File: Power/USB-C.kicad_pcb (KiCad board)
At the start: 2 copper layers, 80 x 30 mm, 27 parts, among them J1 USB_C_Receptacle_PowerOnly_6P, J2 Barrel_Jack_Switch, J3 Barrel_Jack_Switch, J4 Barrel_Jack_Switch, J5 Barrel_Jack_Switch, U1 HUSB237, U2 TPS73801

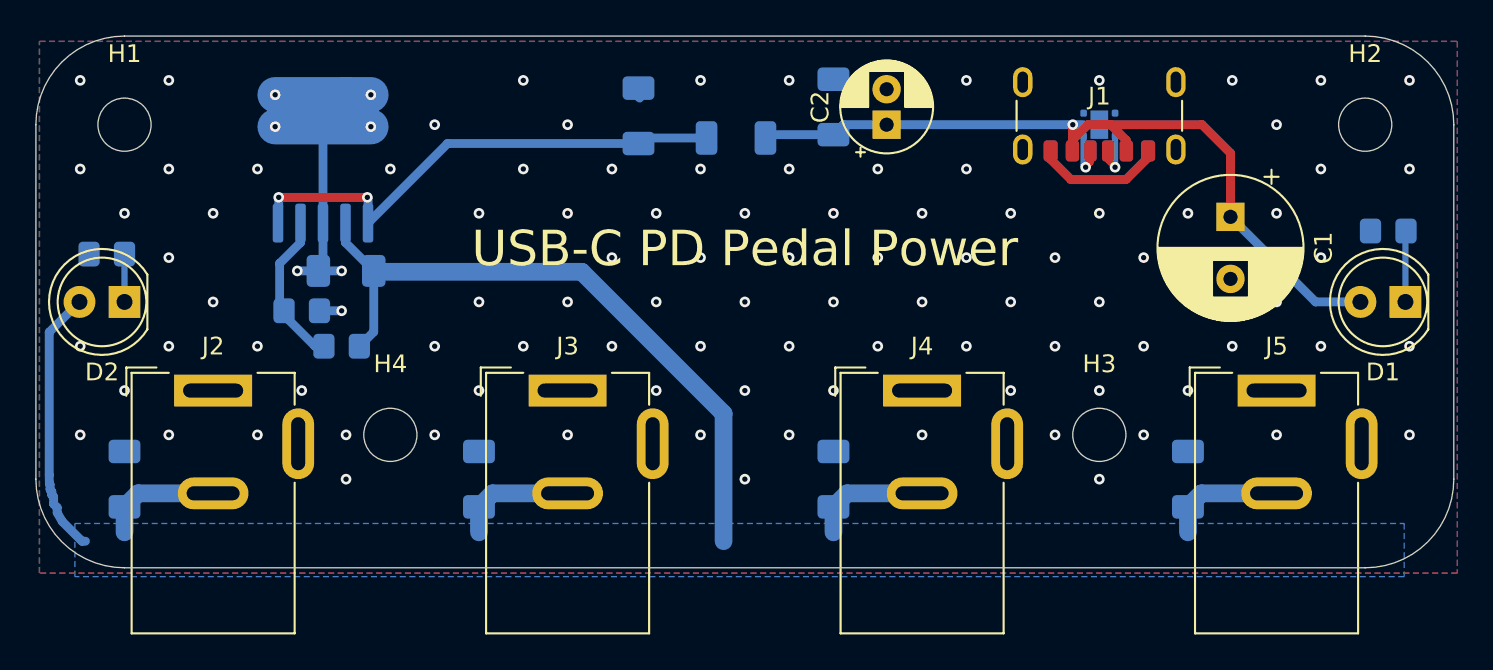
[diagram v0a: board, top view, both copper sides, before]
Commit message: Make a switchable combo version of the USB-PD power board
So this was triggered partly by me noticing that my USB PD sources are
very inconsistent when it comes to 12V output that the original board
requested.

Several of my wall chargers do 15V but not 12V.  Of course, then some of
my battery packs are the reverse, and do 12V but not 15V output.

So there is no single thing that works for all common cases.  But 15V is
the more common option, and is required by the PD specs for anything
that claims to be 45W or more.  12V is entirely optional.

End result: add a switch to pick whether the power board requests 12V or
15V from the USB-C PD source.

And since 15V is now an option, add another LDO, and a switch to make
that LDO generate either 9V or 12V output (as per commit eb97091: "Add a
USB-C pedal power board" that already mentioned this option).

Connect the LDOs to two ports each, which also results in a certain
amount of isolation.

End result: the first two ports always output 9V, while the second two
ports can optionally provide 12V output if your USB-PD source does 15V.

The "switch" is either just a pin header with a jumper, or one of the
small slide switches that I have.  We're not doing anything fancy here.

Signed-off-by: Linus Torvalds <torvalds@linux-foundation.org>
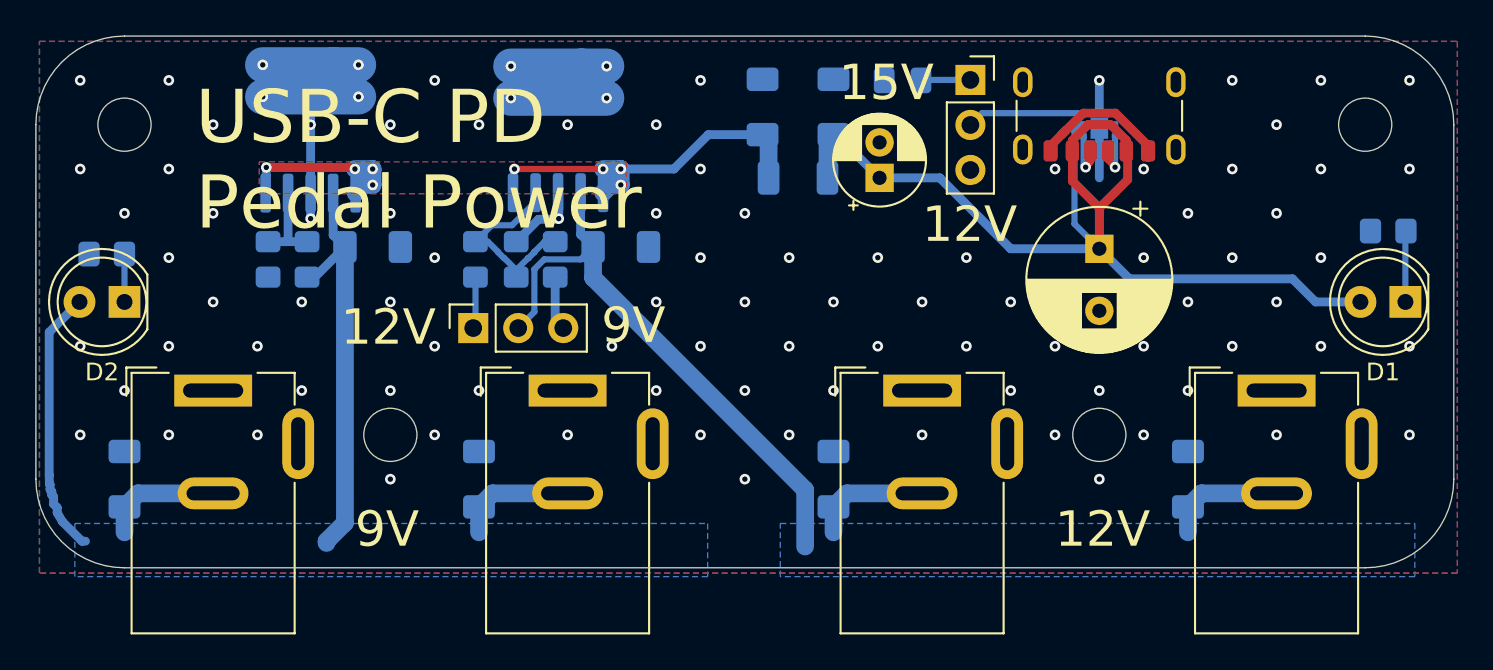
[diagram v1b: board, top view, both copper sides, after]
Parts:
- added C11: 22uF, Capacitor_SMD:C_1206_3216Metric_Pad1.33x1.80mm_HandSolder, B.Cu at (83.0, 61.9)
- added C5: 4.7nF, Capacitor_SMD:C_0805_2012Metric_Pad1.18x1.45mm_HandSolder, B.Cu at (98.9, 52.5)
- added R3: 13k, Resistor_SMD:R_0805_2012Metric_Pad1.20x1.40mm_HandSolder, B.Cu at (79.3, 62.6)
- added R4: 18k, Resistor_SMD:R_0805_2012Metric_Pad1.20x1.40mm_HandSolder, B.Cu at (74.8, 62.6)
- added R7: 2k, Resistor_SMD:R_0805_2012Metric_Pad1.20x1.40mm_HandSolder, B.Cu at (77.1, 62.6)
- added SW1: 15v12, Connector_PinSocket_2.54mm:PinSocket_1x03_P2.54mm_Vertical, F.Cu at (102.7, 52.5)
- added SW2: 12v9, Connector_PinSocket_2.54mm:PinSocket_1x03_P2.54mm_Vertical, F.Cu at (74.7, 66.5)
- added U2: TPS73801, Package_TO_SOT_SMD:SOT-223-6, B.Cu at (79.5, 55.7)
- C10: renamed from C9; value 10uF -> 22uF
- C6: renamed from C5; value 10uF -> 22uF
- C7: renamed from C6; value 10uF -> 22uF
- C8: renamed from C7; value 10uF -> 22uF
- C9: renamed from C8; value 10uF -> 22uF
- moved C1 7.62 mm to (110.0, 62.0)
- moved C4 7.02 mm to (91.0, 54.0)
- moved R5 5.27 mm to (65.3, 62.6), turned to 90 degrees
- moved FB1 4.16 mm to (93.0, 58.0)
- moved R6 3.47 mm to (63.1, 62.6), turned to -90 degrees
- moved C2 3.03 mm to (97.6, 58.0)
- moved C7 2.02 mm to (69.0, 61.9), turned to 0 degrees
- moved U3 1.83 mm to (65.5, 55.7)
- renumbered R3 to R1, R4 to R2, R1 to R5, R2 to R6, U2 to U3
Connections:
- net FB renamed FB9
- C10 pad 1: +9V -> +12V
- C4 pad 1: +12V -> +15V
- C9 pad 1: +9V -> +12V
- FB1 pad 2: +12V -> +15V
- J4 pad 2: +9V -> +12V
- J5 pad 2: +9V -> +12V
- U1 pad 3: unconnected-(U1-VSET-Pad3) -> Net-(SW1-B)
- U3 pad 1: +12V -> +15V
- U3 pad 5: +12V -> +15V
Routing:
- net +15V: track 0.00 -> 30.6 mm, vias 0 -> 8
- net +9V: track 80.4 -> 51.9 mm
- net +12V: track 28.6 -> 46.2 mm, vias 2 -> 0
- net GND: track 30.7 -> 47.7 mm, vias 104 -> 98
- net VBUS: track 45.4 -> 59.1 mm, vias 1 -> 0
- net FB12: track 0.00 -> 11.2 mm
- net Net-(SW1-B): track 0.00 -> 6.66 mm
- net FB9: track 8.77 -> 4.99 mm
- net Net-(SW2-C): track 0.00 -> 3.50 mm
- net Net-(SW2-A): track 0.00 -> 2.93 mm
- net Net-(SW1-A): track 0.00 -> 2.80 mm
- added copper zone on B.Cu, net +12V
- added copper zone on F.Cu, net +15V
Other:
- board text added: "12V"
- board text added: "15V"
- board text added: "9V"

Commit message: Update USB-C pedal power board a bit more
Testing the old 12V-only board shows that several of my PD power
supplies that claim to only do 5V, 9V and 15V actually do 12V even if
they don't say so on the power supply.

It looks like 12V is common mainly due to Qualcomm Quick Charge (where
it is part of the spec), and so if the PD power supply does that, it
likely does 12V USB-PD too.

But having the switchable option is good regardless, and this adds a
updates the capacitor choices a bit.

I don't really have a great way to test power quality, but waving the
output end of the guitar pedal power supply next to a guitar cable that
is connected to the amp at the other end seems to be a good first
sanity-check.

And according to that simple check, the first (12V-only) pedal board is
fine.  Better than a commercial one I have around, in fact.  So these
may be quite usable.

Signed-off-by: Linus Torvalds <torvalds@linux-foundation.org>
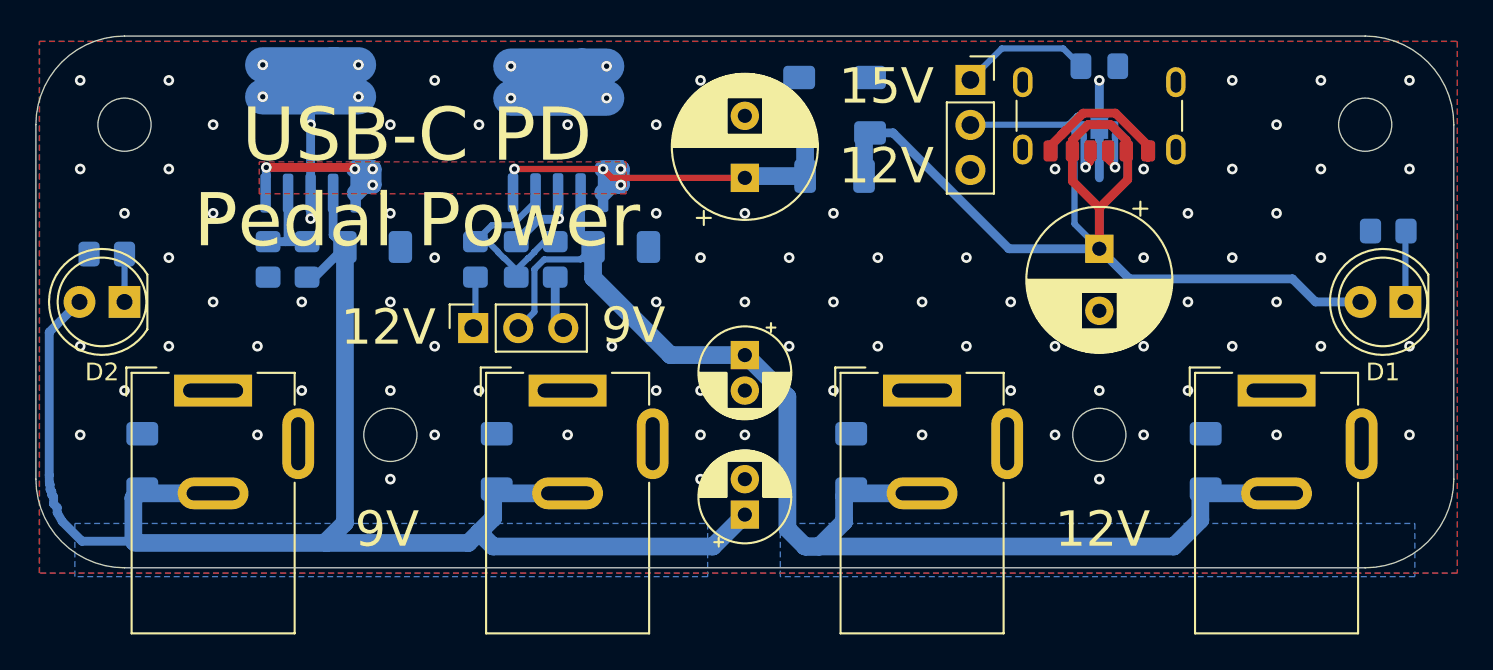
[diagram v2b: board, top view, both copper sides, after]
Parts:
- added C12: 47uF, Capacitor_THT:CP_Radial_D5.0mm_P2.00mm, F.Cu at (90.0, 77.0)
- added C13: 47uF, Capacitor_THT:CP_Radial_D5.0mm_P2.00mm, F.Cu at (90.0, 68.0)
- C4: renamed from C2; value 47uF -> 100uF; footprint Capacitor_THT:CP_Radial_D5.0mm_P2.00mm -> Capacitor_THT:CP_Radial_D8.0mm_P3.50mm
- moved C5 11.1 mm to (110.0, 51.7), turned to 0 degrees
- moved C4 7.60 mm to (90.0, 58.0)
- moved C2 2.06 mm to (97.1, 53.9)
- moved C3 2.06 mm to (93.1, 53.9)
- moved FB1 2.06 mm to (95.1, 57.9)
- moved C10 1.41 mm to (116.0, 74.0)
- moved C6 1.41 mm to (56.0, 74.0)
- moved C8 1.41 mm to (76.0, 74.0)
- moved C9 1.41 mm to (96.0, 74.0)
- renumbered C3 to C2, C4 to C3, R5 to R3, R3 to R4, R4 to R5
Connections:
- C4 pad 1: VBUS -> +15V
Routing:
- net +9V: track 51.9 -> 90.8 mm
- net +12V: track 46.2 -> 72.6 mm
- net Net-(SW1-A): track 2.80 -> 7.39 mm
- net +15V: track 30.6 -> 34.0 mm
- net VBUS: track 59.1 -> 57.1 mm
- net GND: vias 98 -> 96

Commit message: Do the ferrite bead on incoming power ground on the power board too
So I was looking at noise on my 5V test-board, and comparing the USB-C
power board to the Donner "real" guitar pedal power supply I have.  And
while my USB-C power board looks a bit better than the Donner on my
scope, I do see what very much looks like switching noise.

And I was comparing the VGND base board with the 5V one, and the bypass
signal on the VGND board really does look noticeably much better.  So
while that ferrite bead on the incoming ground started out as a "let's
try this", I'm becoming fairly convinced that it's meaningful.

Now, it probably isn't something that affects sound, because obviously
the bead just affects high-frequency noise.  We're definitely not
talking audio frequencies here.  But when it's visible on the scope, it
affects my ability to make judgment calls about other issues, so it
matters to me.

And who knows - noisy power might have an indirect effect on the opamps
or other chips, so cleaning it up can't be bad in general.

End result: let's just do the ferrite bead on the power supply board the
same way I did it on the 5V base board.  Separating those ground lines
just looks like the right thing to do and makes the board layout look
better anyway.

I don't know enough to actually believe in separate digital and analog
grounds, and I just do ground pours everywhere I can.  But filtering
incoming power lines is the kind of basic hygiene I can strive for.

Signed-off-by: Linus Torvalds <torvalds@linux-foundation.org>
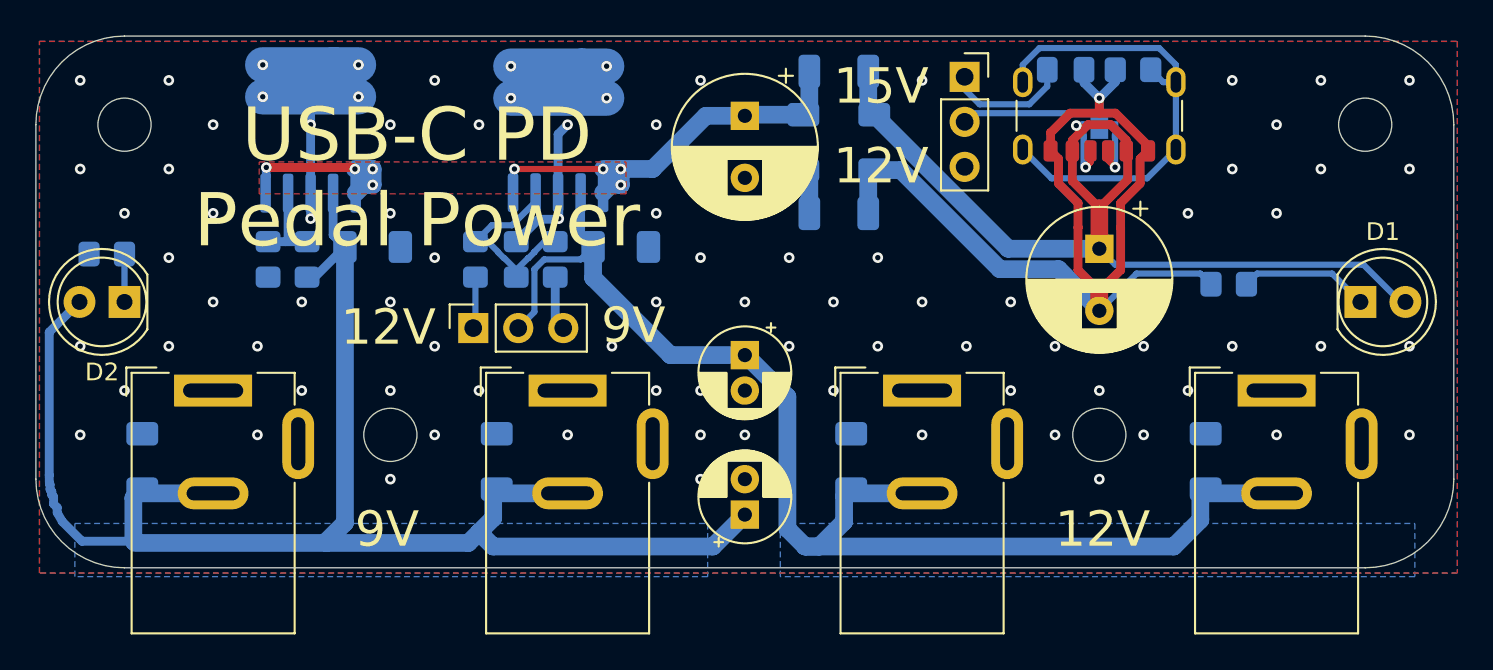
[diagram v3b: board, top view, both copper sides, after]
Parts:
- added FB2: FerriteBead, Inductor_SMD:L_1206_3216Metric_Pad1.22x1.90mm_HandSolder, B.Cu at (95.3, 60.0)
- added R8: 10R, Resistor_SMD:R_0805_2012Metric_Pad1.20x1.40mm_HandSolder, B.Cu at (111.9, 51.9)
- moved R1 9.49 mm to (117.3, 64.0)
- moved FB1 5.90 mm to (95.3, 52.0)
- moved C4 3.50 mm to (90.0, 54.5), turned to -90 degrees
- moved D1 2.54 mm to (124.7, 65.0), turned to 0 degrees
- moved C2 2.11 mm to (97.3, 56.0), turned to -90 degrees
- moved C3 2.11 mm to (93.3, 56.0), turned to -90 degrees
- moved C5 1.91 mm to (108.1, 51.9)
- moved SW1 0.37 mm to (102.4, 52.3)
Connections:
- C1 pad 2: GND -> GNDBUS
- C2 pad 2: GND -> GNDBUS
- C5 pad 2: GND -> GNDBUS
- J1 pad A12: GND -> GNDBUS
- J1 pad B12: GND -> GNDBUS
- J1 pad S1: GND -> SHIELD
- R1 pad 2: GND -> GNDBUS
- U1 pad 7: GND -> GNDBUS
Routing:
- net GNDBUS: track 0.00 -> 59.0 mm, vias 0 -> 1
- net SHIELD: track 0.00 -> 27.2 mm
- net GND: track 47.7 -> 40.3 mm, vias 96 -> 86
- net VBUS: track 57.1 -> 52.8 mm, vias 0 -> 1
- net Net-(D1-K): track 4.01 -> 7.34 mm
- net FB12: track 11.2 -> 10.2 mm
- net +15V: track 34.0 -> 33.1 mm

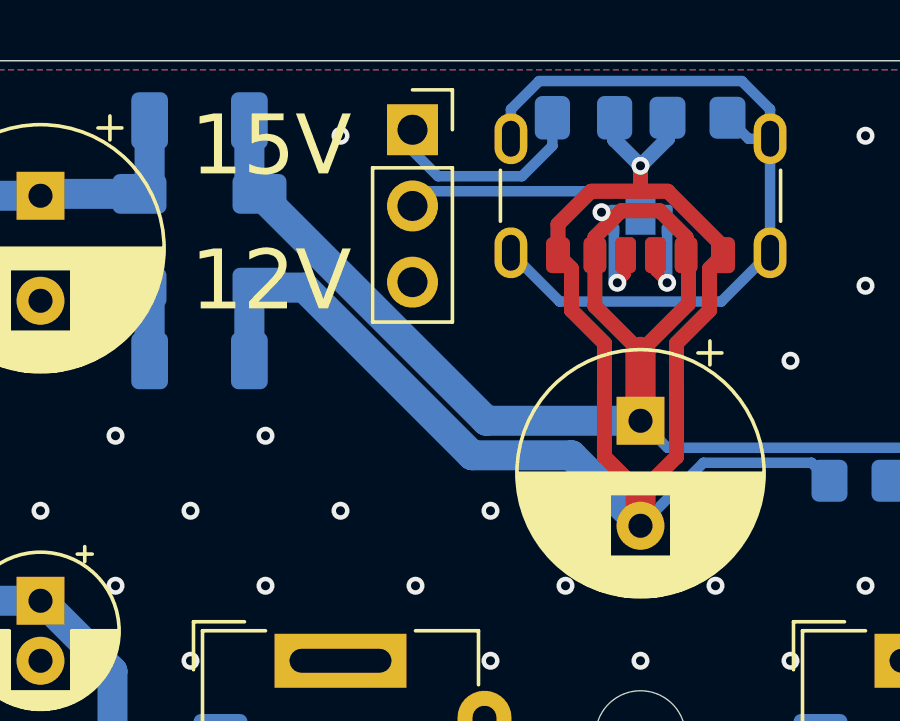
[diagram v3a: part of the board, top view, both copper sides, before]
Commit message: USB-C power board: do the common mode choke thing
It should probably go before the initial capacitor, but that would make
me have to lay out the board anew for this part, so I'm just doing a
minimal trial.  Any high-frequency common mode noise will bypass the cap
anyway, methinks.

Will this make any difference? Probably not, but let's see.

Signed-off-by: Linus Torvalds <torvalds@linux-foundation.org>
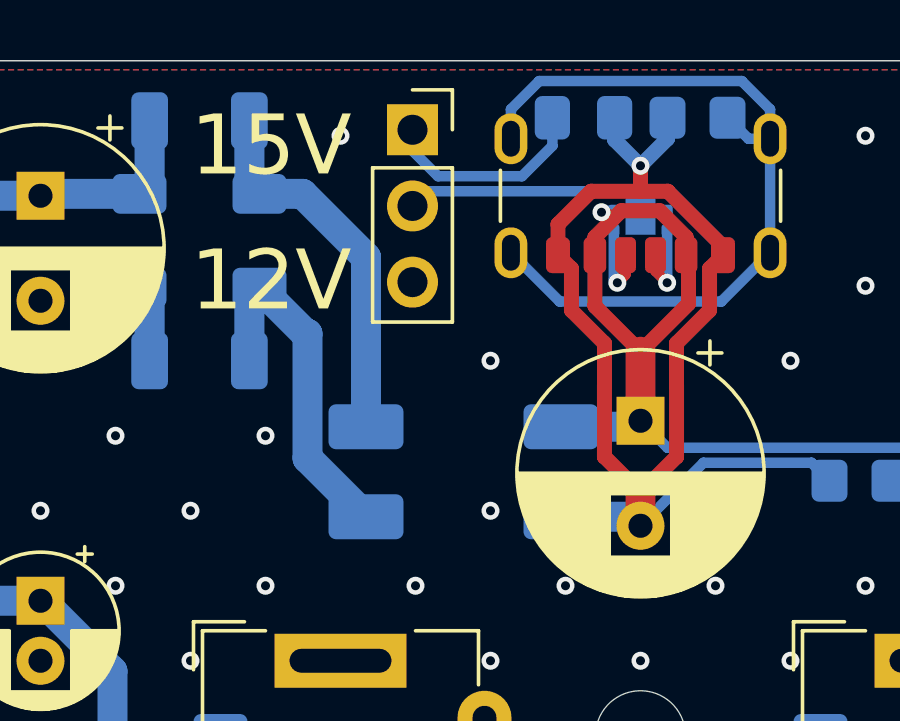
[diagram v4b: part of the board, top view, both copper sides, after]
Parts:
- added FL1: ACM7060, Inductor_SMD:L_CommonModeChoke_TDK_ACM7060, B.Cu at (104.1, 63.7)
- renumbered R8 to R3, R3 to R4, R4 to R5, R5 to R6, R6 to R7, R7 to R8
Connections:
- C2 pad 1: VBUS -> Net-(C2-Pad1)
- C2 pad 2: GNDBUS -> Net-(C2-Pad2)
- FB1 pad 1: VBUS -> Net-(C2-Pad1)
- FB2 pad 1: GNDBUS -> Net-(C2-Pad2)
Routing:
- net GNDBUS: track 59.0 -> 43.2 mm
- net VBUS: track 52.8 -> 37.1 mm
- net Net-(C2-Pad1): track 0.00 -> 12.7 mm
- net Net-(C2-Pad2): track 0.00 -> 11.7 mm
